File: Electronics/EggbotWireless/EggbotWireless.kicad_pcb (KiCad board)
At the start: 2 copper layers, 118 x 40 mm, 76 parts, among them J1 BATT, J2 Conn_01x03_Male, J3 USB_B_Micro, J4 AVR-ISP-6, J5 Conn_01x03_Female, J6 Conn_01x05_Male, M1 , M2 , M3 Motor_Servo, Q1 FDD8447L, Q2 2N7002, Q3 AOD403, Q4 2N7002, Q5 S8050, Q6 S8050, SW1 , U1 TPS62203DBV, U2 ATmega328P-AU, U3 DW01, U4 DMG4800LSD, U5 FT232RL, U6 LTC4054ES5-4.2, U7 ESP-12E, U8 LM3478, Y1 16MHz

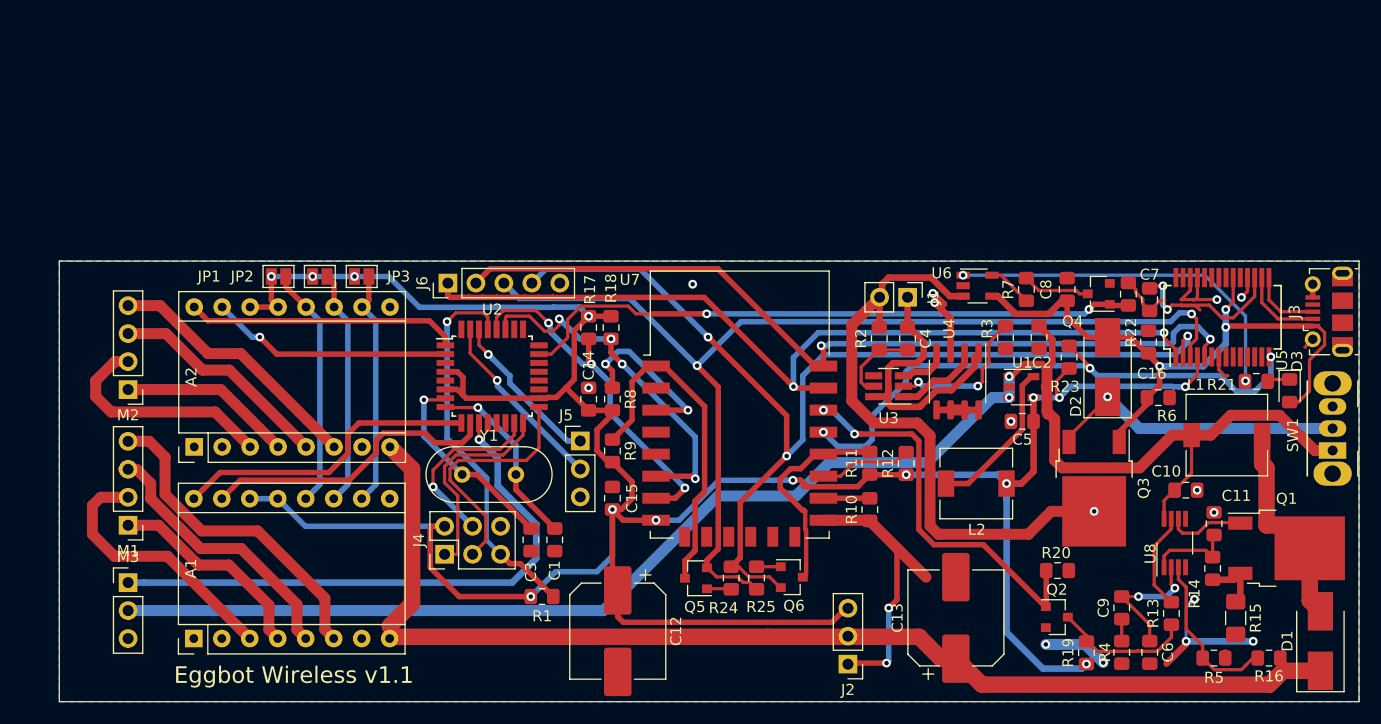
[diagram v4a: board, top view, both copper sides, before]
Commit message: fix issue with ft232rl being powered with rx/tx board v1.1b
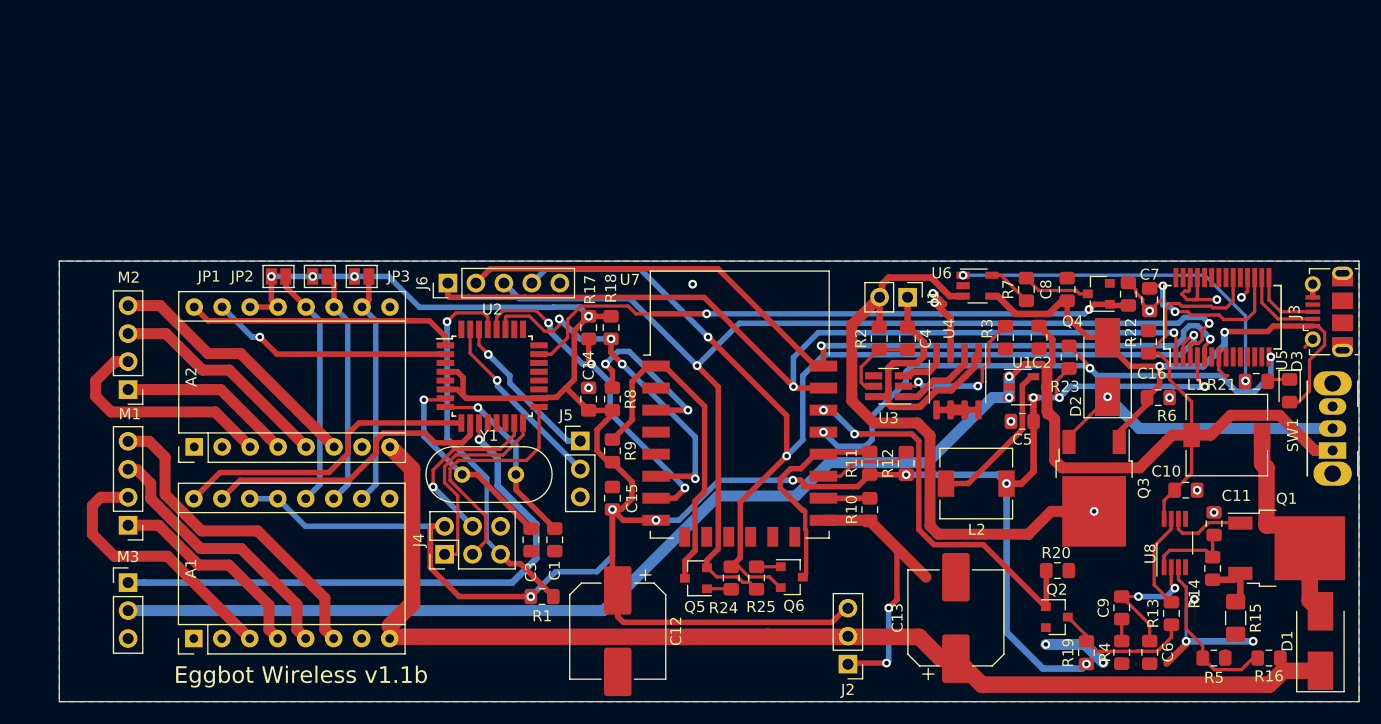
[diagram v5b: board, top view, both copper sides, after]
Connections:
- C16 pad 2: VBUS -> +5V
- U5 pad 20: VBUS -> +5V
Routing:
- net +5V: track 144.9 -> 168.0 mm
- net VBUS: track 58.1 -> 53.4 mm, vias 3 -> 2
- net +3V3: track 247.6 -> 249.2 mm
- net RTS_USB: track 96.7 -> 98.1 mm
- net Net-(C7-Pad2): track 16.8 -> 15.5 mm
- net DTR_USB: track 97.0 -> 98.0 mm
- net TXD_USB: track 78.6 -> 79.1 mm
- net GND: track 74.9 -> 74.7 mm, vias 16 -> 18
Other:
- board text added: "Eggbot Wireless v1.1b"
- board text removed: "Eggbot Wireless v1.1"

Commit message: board v1.2 use p-mosfet for charge enable/disable use sleep instead of pwren connect battery to esp adc via voltage divider
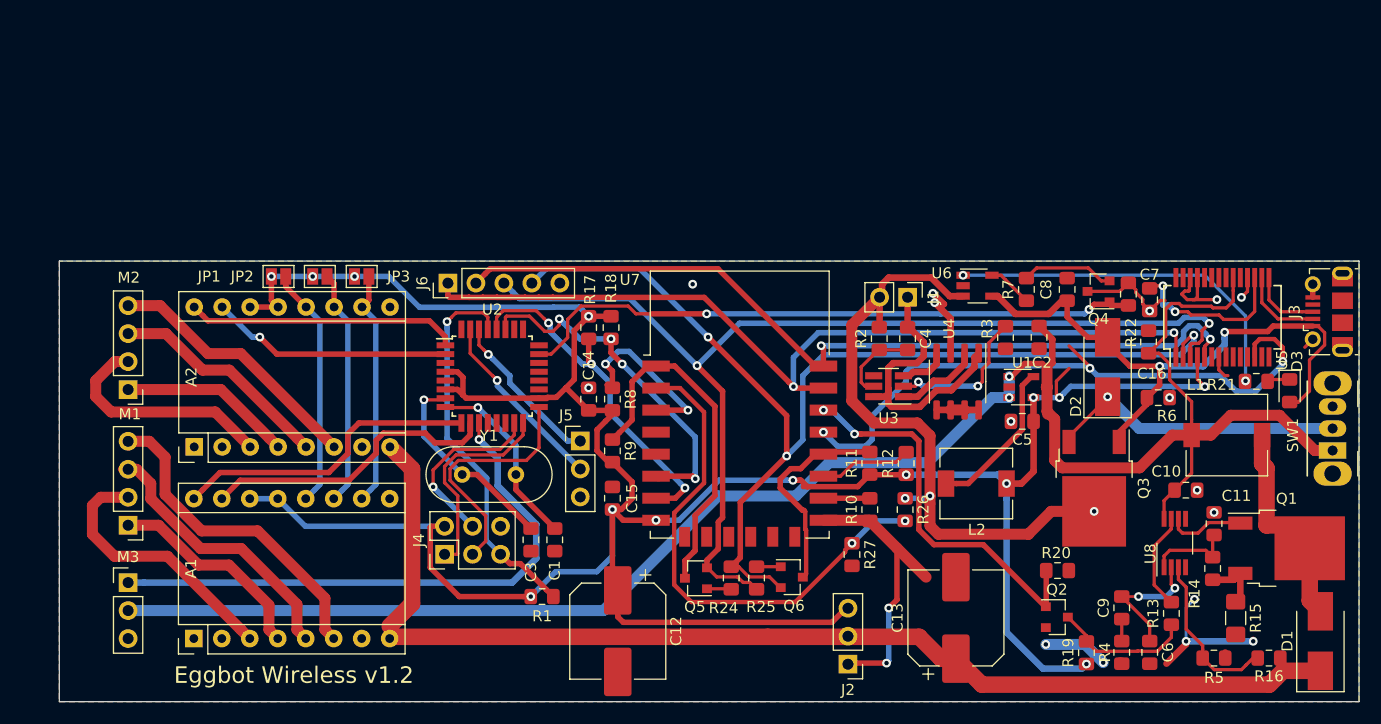
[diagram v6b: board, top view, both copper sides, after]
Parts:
- removed R23: 10K, Resistor_SMD:R_0805_2012Metric_Pad1.15x1.40mm_HandSolder
- added R26: 12K, Resistor_SMD:R_0805_2012Metric_Pad1.15x1.40mm_HandSolder, F.Cu at (96.2, 60.1)
- added R27: 3K, Resistor_SMD:R_0805_2012Metric_Pad1.15x1.40mm_HandSolder, F.Cu at (91.3, 64.2)
- Q4: value 2N7002 -> IRLML6402
- moved Q4 0.23 mm to (113.7, 40.3)
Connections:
- net Net-(J1-Pad2) renamed BATT
- Q4 pad 2: GND -> Net-(Q4-Pad2)
- Q4 pad 3: Net-(Q4-Pad3) -> GND
- R7 pad 2: Net-(Q4-Pad3) -> Net-(Q4-Pad2)
- U5 pad 12: (no net) -> SLEEP
- U5 pad 14: PWREN -> (no net)
- U7 pad 19: PWREN -> SLEEP
- U7 pad 2: (no net) -> Net-(R26-Pad2)
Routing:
- net SLEEP: track 0.00 -> 57.6 mm, vias 0 -> 3
- net PWREN: track 52.2 -> 0.00 mm, vias 3 -> 0
- net Net-(R26-Pad2): track 0.00 -> 46.8 mm, vias 0 -> 2
- net Net-(Q4-Pad2): track 0.00 -> 8.42 mm
- net Net-(Q4-Pad3): track 6.46 -> 0.00 mm
- net GND: track 74.7 -> 79.1 mm
- net BATT: track 55.3 -> 57.7 mm, vias 1 -> 3
- net ESPRST: track 31.4 -> 32.7 mm
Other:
- board text added: "Eggbot Wireless v1.2"
- board text removed: "Eggbot Wireless v1.1b"

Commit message: clean up pcb a little bit
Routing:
- net +3V3: track 249.2 -> 246.0 mm, vias 14 -> 13
- net SLEEP: track 57.6 -> 54.8 mm, vias 3 -> 2

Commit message: better mosfets heat dissipation v1.2b
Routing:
- net Net-(D1-Pad2): track 19.3 -> 19.6 mm, vias 0 -> 1
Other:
- board text added: "Eggbot Wireless v1.2b"
- board text removed: "Eggbot Wireless v1.2"
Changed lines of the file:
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@@
     (thickness 1.6)
     (drawings 6)
-    (tracks 930)
+    (tracks 933)
     (zones 0)
     (modules 77)
@@
     (add_net +12V)
   )
+  (module Package_TO_SOT_SMD:TO-252-2 (layer F.Cu)
+    (at 130.789 63.603)
+    (descr "TO-252 / DPAK SMD package, http://www.infineon.com/cms/en/product/packages/PG-TO252/PG-TO252-3-1/")
+    (tags "DPAK TO-252 DPAK-3 TO-252-3 SOT-428")
+    (attr smd)
+    (fp_text reference Q1 (at 0 -4.5) (layer F.SilkS)
+      (effects (font (size 1 1) (thickness 0.15)))
+    )
+    (fp_text value FDD8447L (at 0 4.5) (layer F.Fab)
+      (effects (font (size 1 1) (thickness 0.15)))
+    )
+    (fp_line (start 3.95 -2.7) (end 4.95 -2.7) (layer F.Fab) (width 0.1))
+    (fp_line (start 4.95 -2.7) (end 4.95 2.7) (layer F.Fab) (width 0.1))
+    (fp_line (start 4.95 2.7) (end 3.95 2.7) (layer F.Fab) (width 0.1))
+    (fp_line (start 3.95 -3.25) (end 3.95 3.25) (layer F.Fab) (width 0.1))
+    (fp_line (start 3.95 3.25) (end -2.27 3.25) (layer F.Fab) (width 0.1))
+    (fp_line (start -2.27 3.25) (end -2.27 -2.25) (layer F.Fab) (width 0.1))
+    (fp_line (start -2.27 -2.25) (end -1.27 -3.25) (layer F.Fab) (width 0.1))
+    (fp_line (start -1.27 -3.25) (end 3.95 -3.25) (layer F.Fab) (width 0.1))
+    (fp_line (start -1.865 -2.655) (end -4.97 -2.655) (layer F.Fab) (width 0.1))
+    (fp_line (start -4.97 -2.655) (end -4.97 -1.905) (layer F.Fab) (width 0.1))
+    (fp_line (start -4.97 -1.905) (end -2.27 -1.905) (layer F.Fab) (width 0.1))
+    (fp_line (start -2.27 1.905) (end -4.97 1.905) (layer F.Fab) (width 0.1))
+    (fp_line (start -4.97 1.905) (end -4.97 2.655) (layer F.Fab) (width 0.1))
+    (fp_line (start -4.97 2.655) (end -2.27 2.655) (layer F.Fab) (width 0.1))
+    (fp_line (start -0.97 -3.45) (end -2.47 -3.45) (layer F.SilkS) (width 0.12))
+    (fp_line (start -2.47 -3.45) (end -2.47 -3.18) (layer F.SilkS) (width 0.12))
+    (fp_line (start -2.47 -3.18) (end -5.3 -3.18) (layer F.SilkS) (width 0.12))
+    (fp_line (start -0.97 3.45) (end -2.47 3.45) (layer F.SilkS) (width 0.12))
+    (fp_line (start -2.47 3.45) (end -2.47 3.18) (layer F.SilkS) (width 0.12))
+    (fp_line (start -2.47 3.18) (end -3.57 3.18) (layer F.SilkS) (width 0.12))
+    (fp_line (start -5.55 -3.5) (end -5.55 3.5) (layer F.CrtYd) (width 0.05))
+    (fp_line (start -5.55 3.5) (end 5.55 3.5) (layer F.CrtYd) (width 0.05))
+    (fp_line (start 5.55 3.5) (end 5.55 -3.5) (layer F.CrtYd) (width 0.05))
+    (fp_line (start 5.55 -3.5) (end -5.55 -3.5) (layer F.CrtYd) (width 0.05))
+    (fp_text user %R (at 0 0) (layer F.Fab)
+      (effects (font (size 1 1) (thickness 0.15)))
+    )
+    (pad 1 smd rect (at -4.2 -2.28) (size 2.2 1.2) (layers F.Cu F.Paste F.Mask)
+      (net 30 "Net-(Q1-Pad1)"))
+    (pad 3 smd rect (at -4.2 2.28) (size 2.2 1.2) (layers F.Cu F.Paste F.Mask)
+      (net 29 "Net-(Q1-Pad3)"))
+    (pad 2 smd rect (at 2.1 0) (size 6.4 5.8) (layers F.Cu F.Mask)
+      (net 7 "Net-(D1-Pad2)"))
+    (pad "" smd rect (at 3.775 1.525) (size 3.05 2.75) (layers F.Paste))
+    (pad "" smd rect (at 0.425 -1.525) (size 3.05 2.75) (layers F.Paste))
+    (pad "" smd rect (at 3.775 -1.525) (size 3.05 2.75) (layers F.Paste))
+    (pad "" smd rect (at 0.425 1.525) (size 3.05 2.75) (layers F.Paste))
+    (model ${KISYS3DMOD}/Package_TO_SOT_SMD.3dshapes/TO-252-2.wrl
+      (at (xyz 0 0 0))
+      (scale (xyz 1 1 1))
+      (rotate (xyz 0 0 0))
+    )
+  )
   (module Package_SO:SSOP-28_5.3x10.2mm_P0.65mm (layer F.Cu)
     (at 124.964 42.628 90)
@@
     )
   )
-  (module Package_TO_SOT_SMD:TO-252-2 (layer F.Cu)
-    (at 130.789 63.603)
-    (descr "TO-252 / DPAK SMD package, http://www.infineon.com/cms/en/product/packages/PG-TO252/PG-TO252-3-1/")
-    (tags "DPAK TO-252 DPAK-3 TO-252-3 SOT-428")
-    (attr smd)
-    (fp_text reference Q1 (at 0 -4.5) (layer F.SilkS)
-      (effects (font (size 1 1) (thickness 0.15)))
-    )
-    (fp_text value FDD8447L (at 0 4.5) (layer F.Fab)
-      (effects (font (size 1 1) (thickness 0.15)))
-    )
-    (fp_line (start 3.95 -2.7) (end 4.95 -2.7) (layer F.Fab) (width 0.1))
-    (fp_line (start 4.95 -2.7) (end 4.95 2.7) (layer F.Fab) (width 0.1))
-    (fp_line (start 4.95 2.7) (end 3.95 2.7) (layer F.Fab) (width 0.1))
-    (fp_line (start 3.95 -3.25) (end 3.95 3.25) (layer F.Fab) (width 0.1))
-    (fp_line (start 3.95 3.25) (end -2.27 3.25) (layer F.Fab) (width 0.1))
-    (fp_line (start -2.27 3.25) (end -2.27 -2.25) (layer F.Fab) (width 0.1))
-    (fp_line (start -2.27 -2.25) (end -1.27 -3.25) (layer F.Fab) (width 0.1))
-    (fp_line (start -1.27 -3.25) (end 3.95 -3.25) (layer F.Fab) (width 0.1))
-    (fp_line (start -1.865 -2.655) (end -4.97 -2.655) (layer F.Fab) (width 0.1))
-    (fp_line (start -4.97 -2.655) (end -4.97 -1.905) (layer F.Fab) (width 0.1))
-    (fp_line (start -4.97 -1.905) (end -2.27 -1.905) (layer F.Fab) (width 0.1))
-    (fp_line (start -2.27 1.905) (end -4.97 1.905) (layer F.Fab) (width 0.1))
-    (fp_line (start -4.97 1.905) (end -4.97 2.655) (layer F.Fab) (width 0.1))
-    (fp_line (start -4.97 2.655) (end -2.27 2.655) (layer F.Fab) (width 0.1))
-    (fp_line (start -0.97 -3.45) (end -2.47 -3.45) (layer F.SilkS) (width 0.12))
-    (fp_line (start -2.47 -3.45) (end -2.47 -3.18) (layer F.SilkS) (width 0.12))
-    (fp_line (start -2.47 -3.18) (end -5.3 -3.18) (layer F.SilkS) (width 0.12))
-    (fp_line (start -0.97 3.45) (end -2.47 3.45) (layer F.SilkS) (width 0.12))
-    (fp_line (start -2.47 3.45) (end -2.47 3.18) (layer F.SilkS) (width 0.12))
-    (fp_line (start -2.47 3.18) (end -3.57 3.18) (layer F.SilkS) (width 0.12))
-    (fp_line (start -5.55 -3.5) (end -5.55 3.5) (layer F.CrtYd) (width 0.05))
-    (fp_line (start -5.55 3.5) (end 5.55 3.5) (layer F.CrtYd) (width 0.05))
-    (fp_line (start 5.55 3.5) (end 5.55 -3.5) (layer F.CrtYd) (width 0.05))
-    (fp_line (start 5.55 -3.5) (end -5.55 -3.5) (layer F.CrtYd) (width 0.05))
-    (fp_text user %R (at 0 0) (layer F.Fab)
-      (effects (font (size 1 1) (thickness 0.15)))
-    )
-    (pad 1 smd rect (at -4.2 -2.28) (size 2.2 1.2) (layers F.Cu F.Paste F.Mask)
-      (net 30 "Net-(Q1-Pad1)"))
-    (pad 3 smd rect (at -4.2 2.28) (size 2.2 1.2) (layers F.Cu F.Paste F.Mask)
-      (net 29 "Net-(Q1-Pad3)"))
-    (pad 2 smd rect (at 2.1 0) (size 6.4 5.8) (layers F.Cu F.Mask)
-      (net 7 "Net-(D1-Pad2)"))
-    (pad "" smd rect (at 3.775 1.525) (size 3.05 2.75) (layers F.Paste))
-    (pad "" smd rect (at 0.425 -1.525) (size 3.05 2.75) (layers F.Paste))
-    (pad "" smd rect (at 3.775 -1.525) (size 3.05 2.75) (layers F.Paste))
-    (pad "" smd rect (at 0.425 1.525) (size 3.05 2.75) (layers F.Paste))
-    (model ${KISYS3DMOD}/Package_TO_SOT_SMD.3dshapes/TO-252-2.wrl
-      (at (xyz 0 0 0))
-      (scale (xyz 1 1 1))
-      (rotate (xyz 0 0 0))
-    )
-  )
   (module Inductor_SMD:L_6.3x6.3_H3 (layer F.Cu)
     (at 102.614 57.728)
@@
   (gr_line (start 137.364 37.528) (end 137.364 77.528) (layer Edge.Cuts) (width 0.05))
   (gr_line (start 19.364 37.528) (end 137.364 37.528) (layer Edge.Cuts) (width 0.05))
-  (gr_text "Eggbot Wireless v1.2" (at 29.764 75.128) (layer F.SilkS)
+  (gr_text "Eggbot Wireless v1.2b" (at 29.764 75.128) (layer F.SilkS)
     (effects (font (size 1.5 1.5) (thickness 0.3)) (justify left))
   )
@@
   (segment (start 128.564 55.928) (end 128.564 53.328) (width 1.5) (layer F.Cu) (net 7))
   (segment (start 128.964 61.528) (end 128.964 56.328) (width 1.5) (layer F.Cu) (net 7))
+  (via (at 132.889 63.603) (size 0.8) (drill 0.4) (layers F.Cu B.Cu) (net 7))
+  (segment (start 133.183 63.603) (end 132.889 63.603) (width 2) (layer B.Cu) (net 7))
   (segment (start 63.590628 67.366628) (end 64.214 67.99) (width 0.5) (layer F.Cu) (net 8))
   (segment (start 61.222999 64.998999) (end 63.590628 67.366628) (width 0.5) (layer F.Cu) (net 8))
@@
   (segment (start 98.413999 53.377999) (end 98.413999 58.858001) (width 1) (layer F.Cu) (net 68))
   (segment (start 98.413999 58.858001) (end 98.413999 59.488001) (width 1) (layer F.Cu) (net 68))
+  (segment (start 113.577 60.253) (end 113.314 60.253) (width 2) (layer B.Cu) (net 68))
   (segment (start 113.964 39.328) (end 114.714 39.328) (width 0.3) (layer F.Cu) (net 69))
   (segment (start 112.78899 38.15299) (end 113.964 39.328) (width 0.3) (layer F.Cu) (net 69))
